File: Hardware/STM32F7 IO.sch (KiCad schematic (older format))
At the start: 32 parts, among them U16 STM32F765ZGT6, Y3 32.768kHz, Y4 8MHz

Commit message: Fixed merge issues
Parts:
- renumbered C39 to C25, C40 to C26, C38 to C27, C11 to C28, C12 to C29, C13 to C30, C14 to C31, C15 to C32, C16 to C33, C17 to C34, C18 to C35, C19 to C36, C20 to C37, C21 to C38, C22 to C39, C23 to C40, C24 to C41, C41 to C42, C42 to C43, C27 to C44, C28 to C45, D15 to D4, D16 to D5, D17 to D6, R36 to R16, R37 to R17, R38 to R18, R39 to R19, TP39 to TP3, U16 to U9, Y3 to Y1, Y4 to Y2
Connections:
- net PW_GOOD_EXT: no longer names the net of U9.67 (PE14)
- net PW_GOOD_INT: no longer names the net of U9.68 (PE15)
- no-connect marks 58 -> 60

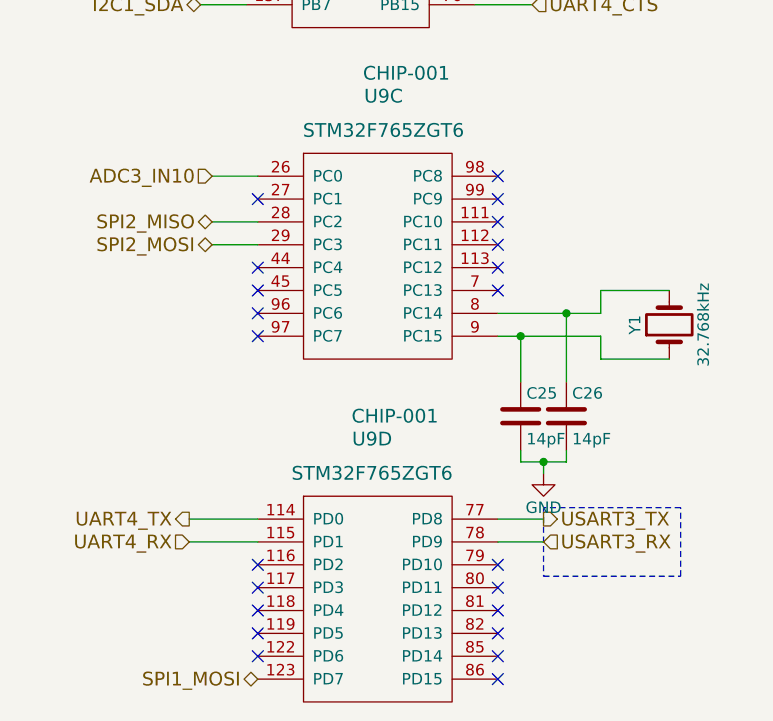
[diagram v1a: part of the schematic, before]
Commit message: Updated schematic
-Changed diode to 0603 diodes
-Changed SD card to proper pinout
-Fixed SPI1 conflict
-Renamed some power nets
-Fixed naming error in IMU NSS
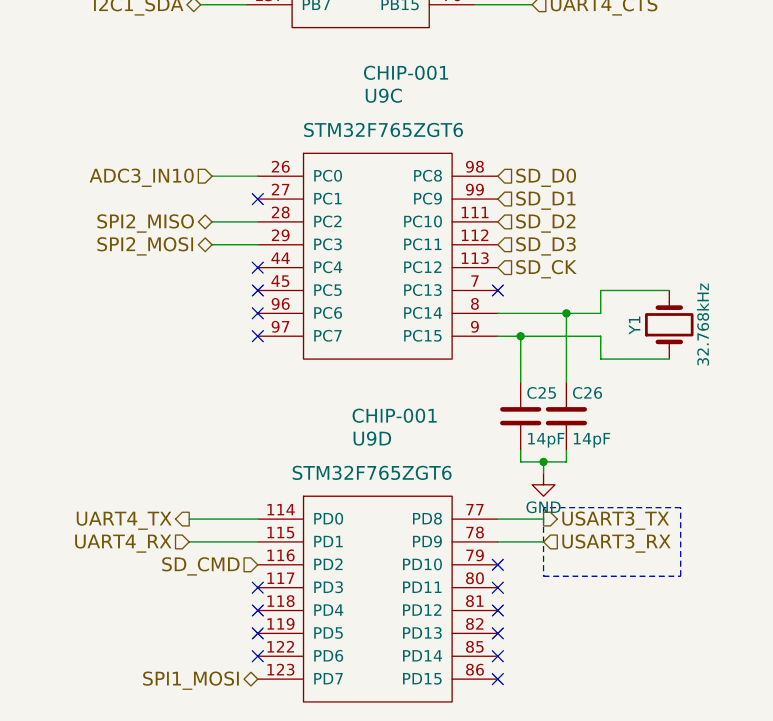
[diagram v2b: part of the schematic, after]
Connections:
- net SD_D2: now reaches U9.111 (PC10)
- net SD_D3: now reaches U9.112 (PC11)
- net SD_CK: now reaches U9.113 (PC12)
- net SD_D0: now reaches U9.98 (PC8)
- net SD_D1: now reaches U9.99 (PC9)
- net SD_CMD: now reaches U9.116 (PD2)
- no-connect marks 60 -> 54
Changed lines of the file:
@@
 NoConn ~ 1700 4900
 NoConn ~ 2750 6200
-NoConn ~ 1700 6100
 NoConn ~ 1700 6200
 NoConn ~ 1700 6300
@@
 $Comp
 L STM32F765ZGT6 U9
-U 4 1 595F8B72
-P 2200 6450
-F 0 "U9" H 2200 7350 60  0000 C CNN
-F 1 "STM32F765ZGT6" H 2200 7200 60  0000 C CNN
-F 2 "Housings_QFP:LQFP-144_20x20mm_Pitch0.5mm" H 3250 6550 60  0001 C CNN
-F 3 "" H 3250 6550 60  0001 C CNN
-F 4 "CHIP-001" H 2300 7450 60  0000 C CNN "part_num"
-	4    2200 6450
-	1    0    0    -1
-$EndComp
-$Comp
-L STM32F765ZGT6 U9
 U 5 1 595F8BE2
 P 6500 2000
@@
 NoConn ~ 1650 2000
 NoConn ~ 1650 2100
-NoConn ~ 2750 4400
-NoConn ~ 2750 4500
-NoConn ~ 2750 4600
-NoConn ~ 2750 4700
-NoConn ~ 2750 4800
 NoConn ~ 2750 4900
 NoConn ~ 2750 6100
@@
 NoConn ~ 7050 2150
 NoConn ~ 7050 2050
+$Comp
+L STM32F765ZGT6 U9
+U 4 1 595F8B72
+P 2200 6450
+F 0 "U9" H 2200 7350 60  0000 C CNN
+F 1 "STM32F765ZGT6" H 2200 7200 60  0000 C CNN
+F 2 "Housings_QFP:LQFP-144_20x20mm_Pitch0.5mm" H 3250 6550 60  0001 C CNN
+F 3 "" H 3250 6550 60  0001 C CNN
+F 4 "CHIP-001" H 2300 7450 60  0000 C CNN "part_num"
+	4    2200 6450
+	1    0    0    -1
+$EndComp
+Text HLabel 2750 4400 2    60   Input ~ 0
+SD_D0
+Text HLabel 2750 4500 2    60   Input ~ 0
+SD_D1
+Text HLabel 2750 4600 2    60   Input ~ 0
+SD_D2
+Text HLabel 2750 4700 2    60   Input ~ 0
+SD_D3
+Text HLabel 2750 4800 2    60   Input ~ 0
+SD_CK
+Text HLabel 1700 6100 0    60   Input ~ 0
+SD_CMD
 $EndSCHEMATC

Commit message: Remapped symbols for KiCAD 5.0.x
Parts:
- C25, C26, C27, C28, C29, C30, C31, C32, C33, C34, C35, C36, C37, C38, C39, C40, C41, C42, C43, C44, C45: symbol C -> Device:C
- D4, D5, D6: symbol LED -> Device:LED
- R16, R17, R18, R19: symbol R -> Device:R
- TP3: symbol TEST -> Connector:TestPoint
- U9: symbol STM32F765ZGT6 -> WARG:STM32F765ZGT6
- Y1, Y2: symbol Crystal -> Device:Crystal
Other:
- moved on the sheet: TP3

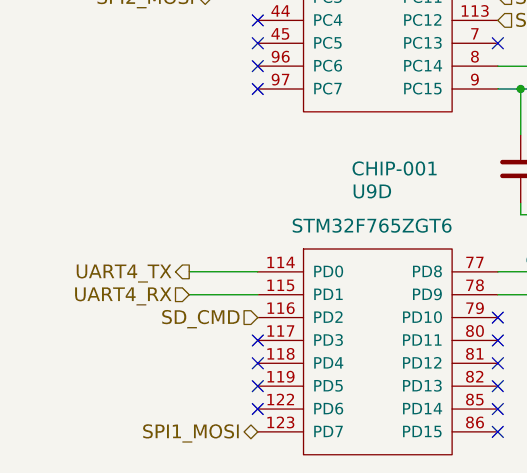
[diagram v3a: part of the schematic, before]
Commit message: Added RSSI, datasheets, INDU-004
Added RSSI input to PPM connector. Added datasheets for most of the components. The filter inductors for the FTDI were labeled as INDU-002, which is a 15uH smps inductor.
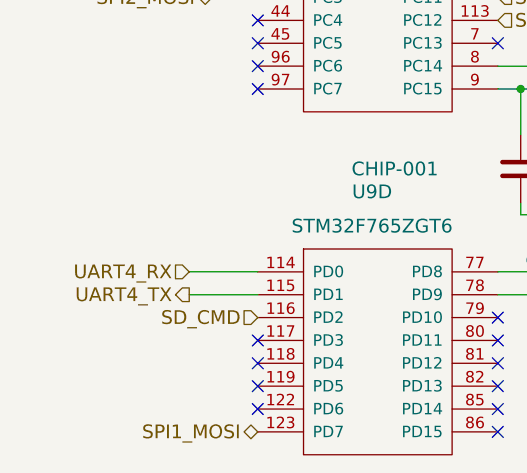
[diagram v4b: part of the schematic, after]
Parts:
- C25, C26, C27, C28, C29, C30, C31, C32, C33, C34, C35, C36, C37, C38, C39, C40, C41, C42, C43, C44, C45: footprint Resistors_SMD:R_0603_HandSoldering -> Capacitors_SMD:C_0603_HandSoldering
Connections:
- net UART4_RX: now also U9.114 (PD0); no longer U9.115 (PD1)
- net UART4_TX: now also U9.115 (PD1); no longer U9.114 (PD0)

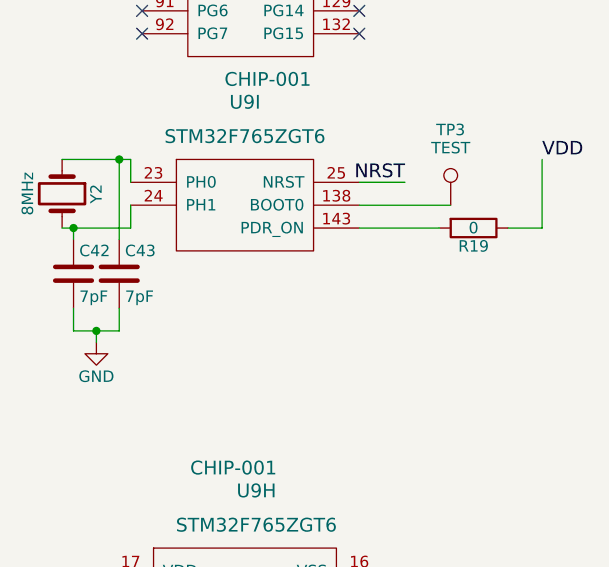
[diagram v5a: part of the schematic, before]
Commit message: Bug fixes, added Isense, changed conn to JST-GH
Added boot0 pull-down resistors. Changed ext_batt to current sense line. Changed spox conn to JST-GH, this will dramatically reduce the required size of the board.
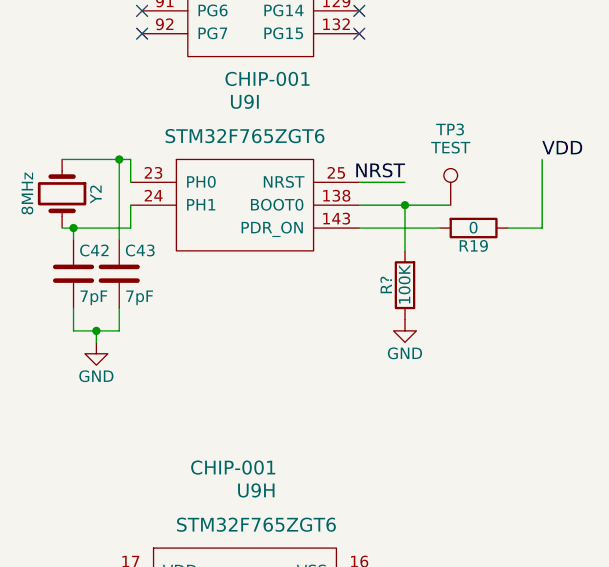
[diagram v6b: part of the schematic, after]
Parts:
- added R?: 100K, Resistors_SMD:R_0603_HandSoldering, symbol Device:R
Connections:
- net GND: now also R?.1
- net at TP3.1, U9.138 (BOOT0): now also R?.2
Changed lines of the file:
@@
 Connection ~ 7850 2500
 Wire Wire Line
-	10450 2900 10050 2900
+	10450 2900 10250 2900
 Connection ~ 6350 4700
 Wire Wire Line
@@
 Wire Wire Line
 	2950 5650 3050 5650
+$Comp
+L Device:R R?
+U 1 1 5CB99043
+P 10250 3250
+F 0 "R?" V 10330 3250 50  0000 C CNN
+F 1 "100K" V 10250 3250 50  0000 C CNN
+F 2 "Resistors_SMD:R_0603_HandSoldering" V 10180 3250 50  0001 C CNN
+F 3 "http://www.yageo.com/documents/recent/PYu-RC_Group_51_RoHS_L_10.pdf" H 10250 3250 50  0001 C CNN
+F 4 "RESS-008" V 10250 3250 60  0001 C CNN "part_num"
+	1    10250 3250
+	-1   0    0    1
+$EndComp
+Connection ~ 10250 2900
+Wire Wire Line
+	10250 2900 10050 2900
+$Comp
+L power:GND #PWR?
+U 1 1 5CB99179
+P 10250 3400
+F 0 "#PWR?" H 10250 3150 50  0001 C CNN
+F 1 "GND" H 10250 3250 50  0000 C CNN
+F 2 "" H 10250 3400 50  0001 C CNN
+F 3 "" H 10250 3400 50  0001 C CNN
+	1    10250 3400
+	1    0    0    -1
+$EndComp
+Wire Wire Line
+	10250 2900 10250 3100
 $EndSCHEMATC

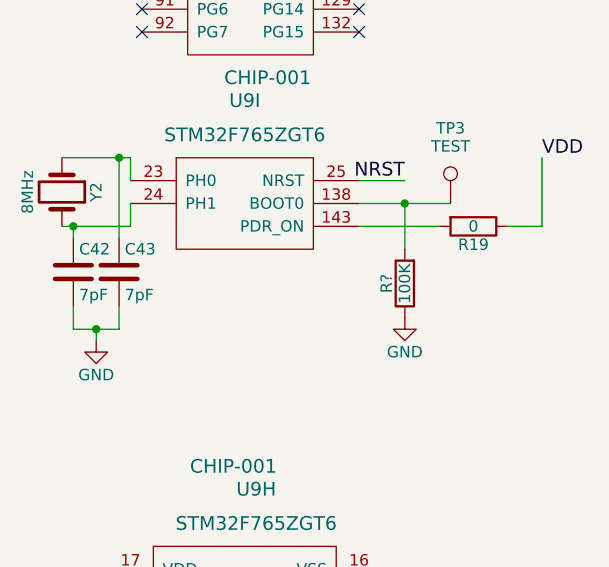
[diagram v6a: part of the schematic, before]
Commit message: Added protection diode to USB
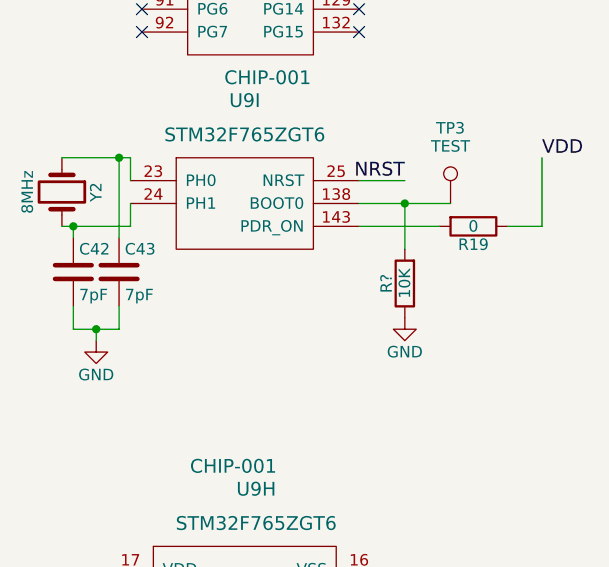
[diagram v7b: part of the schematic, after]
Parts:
- R?: value 100K -> 10K; part_num RESS-008 -> RESS-005
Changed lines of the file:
@@
 P 10250 3250
 F 0 "R?" V 10330 3250 50  0000 C CNN
-F 1 "100K" V 10250 3250 50  0000 C CNN
+F 1 "10K" V 10250 3250 50  0000 C CNN
 F 2 "Resistors_SMD:R_0603_HandSoldering" V 10180 3250 50  0001 C CNN
 F 3 "http://www.yageo.com/documents/recent/PYu-RC_Group_51_RoHS_L_10.pdf" H 10250 3250 50  0001 C CNN
-F 4 "RESS-008" V 10250 3250 60  0001 C CNN "part_num"
+F 4 "RESS-005" V 10250 3250 60  0001 C CNN "part_num"
 	1    10250 3250
 	-1   0    0    1
